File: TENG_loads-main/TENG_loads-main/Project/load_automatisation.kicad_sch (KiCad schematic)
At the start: 30 parts, among them IC1 OPA2145IDR, IC9 OPA145IDBVT, J1 PowerNeg, J12 PH-2X05SG, J13 1757242, J30 1757349, J9 PowerIn, U1 AMS1117-5.0, U2 INA128, U3 AMS1117-5.0

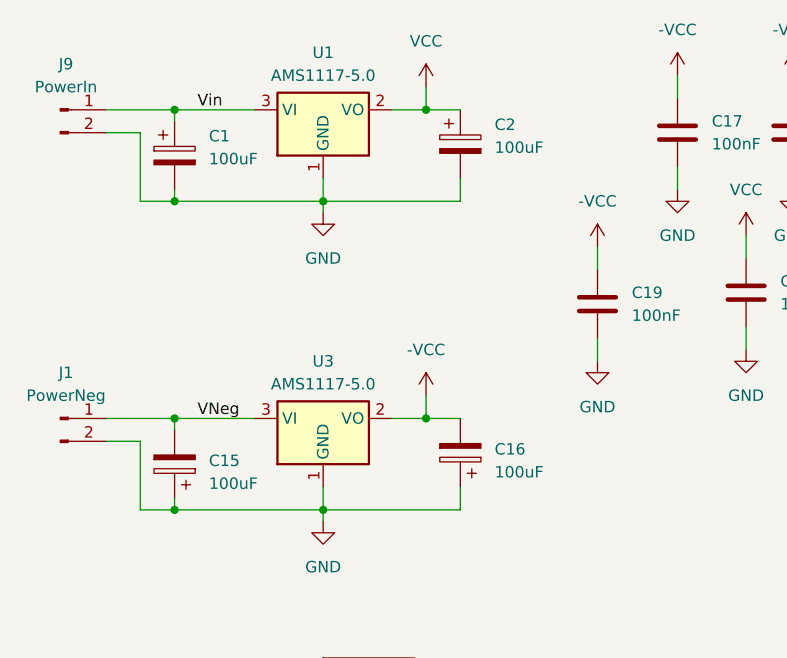
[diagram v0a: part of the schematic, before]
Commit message: Capacitor and relay changes
Capacitor correction and relay ID correction
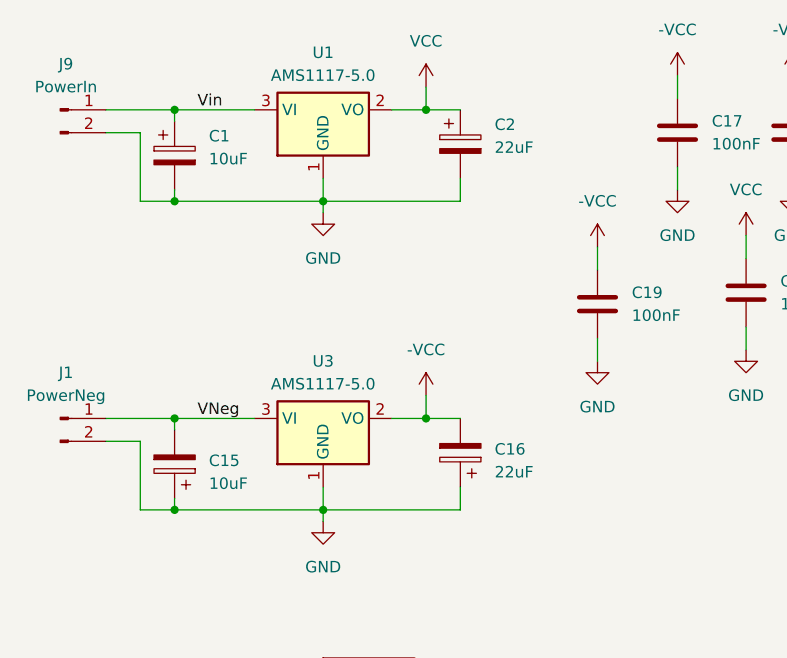
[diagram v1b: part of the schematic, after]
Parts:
- C1, C15: value 100uF -> 10uF
- C16, C2: value 100uF -> 22uF
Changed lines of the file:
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@@
 			)
 		)
-		(property "Value" "100uF"
+		(property "Value" "10uF"
 			(at 43.18 65.6589 0)
 			(effects
@@
 			)
 		)
-		(property "Value" "100uF"
+		(property "Value" "22uF"
 			(at 74.93 64.3889 0)
 			(effects
@@
 			)
 		)
-		(property "Value" "100uF"
+		(property "Value" "22uF"
 			(at 74.93 28.3209 0)
 			(effects
@@
 			)
 		)
-		(property "Value" "100uF"
+		(property "Value" "10uF"
 			(at 43.18 29.5909 0)
 			(effects

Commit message: Updated connections
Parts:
- removed J9: PowerIn, Connector_PinHeader_2.54mm:PinHeader_1x02_P2.54mm_Vertical, symbol Connector:Conn_01x02_Pin
- added J2, J3: 1757242, SamacSys_Parts:1757242, symbol SamacSys_Parts:1757242
- added J4: PowerIn, Connector_PinHeader_2.54mm:PinHeader_1x02_P2.54mm_Vertical, symbol Connector:Conn_01x02_Pin
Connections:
- net GND: now also J2.1, J3.1; no longer J1.2 (Pin_2)
- net Teng+: now also TENG_Connector2.2 (Pin_2); no longer TENG_Connector1.1 (Pin_1)
- net Teng-: now also J13.2, TENG_Connector1.3 (Pin_3), TENG_Connector2.3 (Pin_3); no longer J12.1, J12.3, J12.5
- net Vin: now also J4.1 (Pin_1)
- net TengP_IN: now reaches TENG_Connector2.1 (Pin_1)
- net TengP_IN: now also TENG_Connector1.1 (Pin_1)
- net TengN_IN: now reaches TENG_Connector2.4 (Pin_4)
- net TengN_IN: now also J12.2, J12.7, TENG_Connector1.4 (Pin_4)
- removed net TengN: J12.2, J12.7, J13.2, TENG_Connector1.3 (Pin_3), TENG_Connector1.4 (Pin_4)
- new net: J1.2 (Pin_2), J3.2
- new net: J2.2, J4.2 (Pin_2)
- new net TengN_sw: J12.1, J12.3, J12.5
- no-connect marks 4 -> 0
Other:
- moved on the sheet: C1, C15, C16, C17, C18, C19, C2, C20, C3, C5, H1, H2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

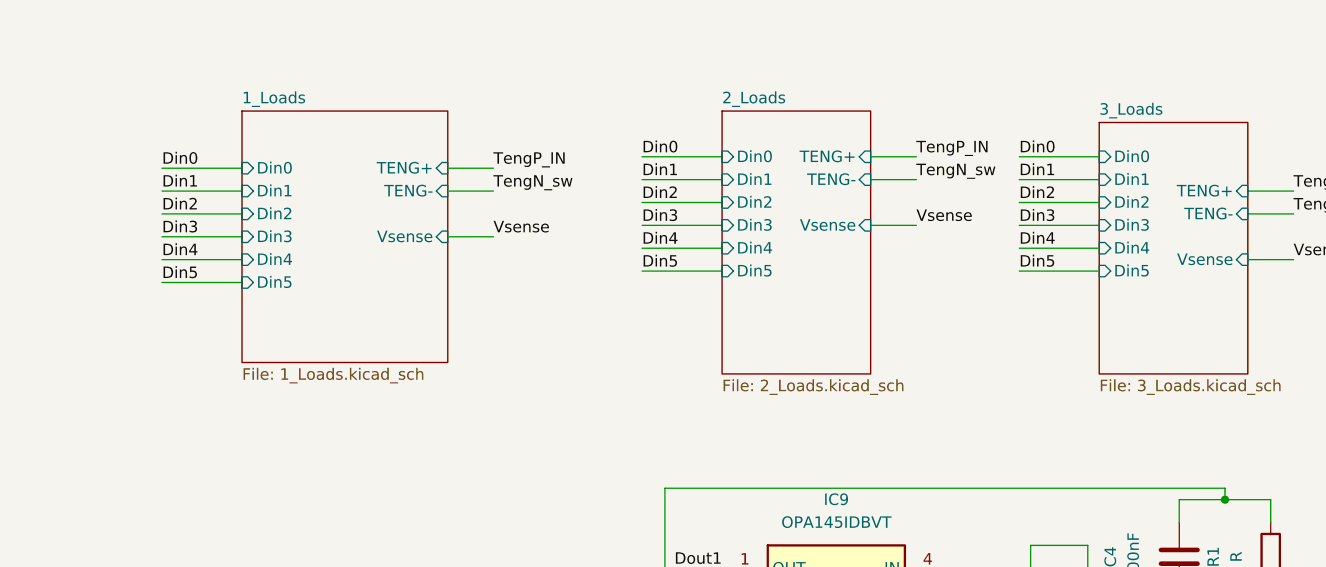
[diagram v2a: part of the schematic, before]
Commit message: Pull Down Resistor and reconnect
Introduced the pull down resistors and reconnect all the unconnected tracks. The position of some items has changed to fit the new components.
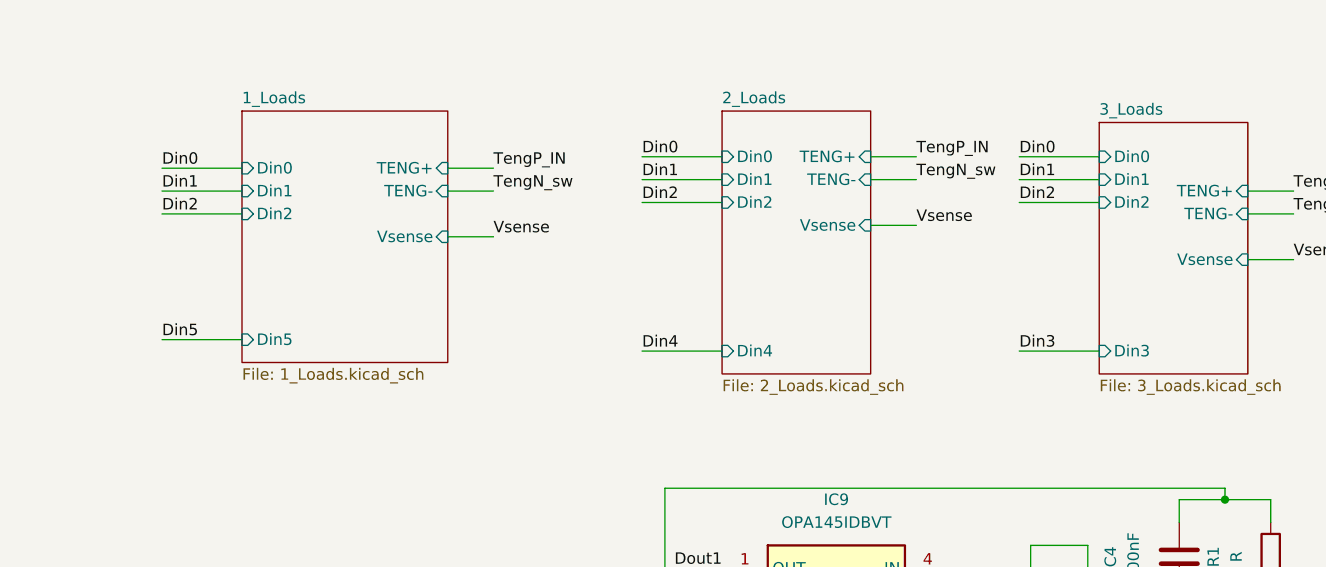
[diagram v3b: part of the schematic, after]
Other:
- sheet 1_Loads ports: added none; removed Din3, Din4
- sheet 2_Loads ports: added none; removed Din3, Din5
- sheet 3_Loads ports: added none; removed Din4, Din5

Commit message: Fix TENg buffer, ans some placements
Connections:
- net Current_Sense2_IN: now also J12.10, J12.8; no longer J12.6
- net Current_Sense2_OUT: now also J12.6; no longer J12.10, J12.8
- net GND: now also J30.9
- net Teng-: no longer IC1.5 (+IN_B)
- net TengN_sw: now also IC1.5 (+IN_B)
